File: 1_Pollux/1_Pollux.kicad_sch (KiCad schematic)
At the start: 0 parts

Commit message: feat: add schematic and pcb basis for right part
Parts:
- added J1: Conn_01x02, Connector_JST:JST_PH_S2B-PH-K_1x02_P2.00mm_Horizontal, symbol Connector_Generic:Conn_01x02
- added SW1: Battery Switch, davidphilipbarr:SPDT_C128955, symbol ScottoKeebs:Placeholder_Switch
- added SW2: LED Switch, davidphilipbarr:SPDT_C128955, symbol ScottoKeebs:Placeholder_Switch
- added SW3: Reset Switch, Button_Switch_SMD:Panasonic_EVQPUL_EVQPUC, symbol ScottoKeebs:Placeholder_Switch
- added U1: Nice_Nano_V2, ScottoKeebs_MCU:Nice_Nano_V2, symbol ScottoKeebs:MCU_Nice_Nano_V2
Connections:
- new net Column 0: U1.5 (2)
- new net Column 1: U1.6 (3)
- new net Column 2: U1.7 (4)
- new net Column 3: U1.8 (5)
- new net Column 4: U1.9 (6)
- new net Column 5: U1.10 (7)
- new net Column 6: U1.11 (8)
- new net Column 7: U1.12 (9)
- new net GND: J1.1 (Pin_1), SW3.1, U1.23 (GND), U1.3 (GND), U1.4 (GND)
- new net LED IN: U1.1
- new net POS: J1.2 (Pin_2), SW1.1
- new net RAW: SW1.2, SW2.1, U1.24 (B+)
- new net RST: SW3.2, U1.22 (RST)
- new net Row 0: U1.20 (21)
- new net Row 1: U1.19 (20)
- new net Row 2: U1.18 (19)
- new net Row 3: U1.17 (18)
- new net Row 4: U1.16 (15)
- new net Row 5: U1.15 (14)
- new net Row 6: U1.14 (16)
- new net Row 7: U1.13 (10)
- new net VDD: SW2.2
- no-connect marks 0 -> 5
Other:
- added sheet Keyswitches (_keyswitches.kicad_sch)
- added sheet LEDs (_leds.kicad_sch)

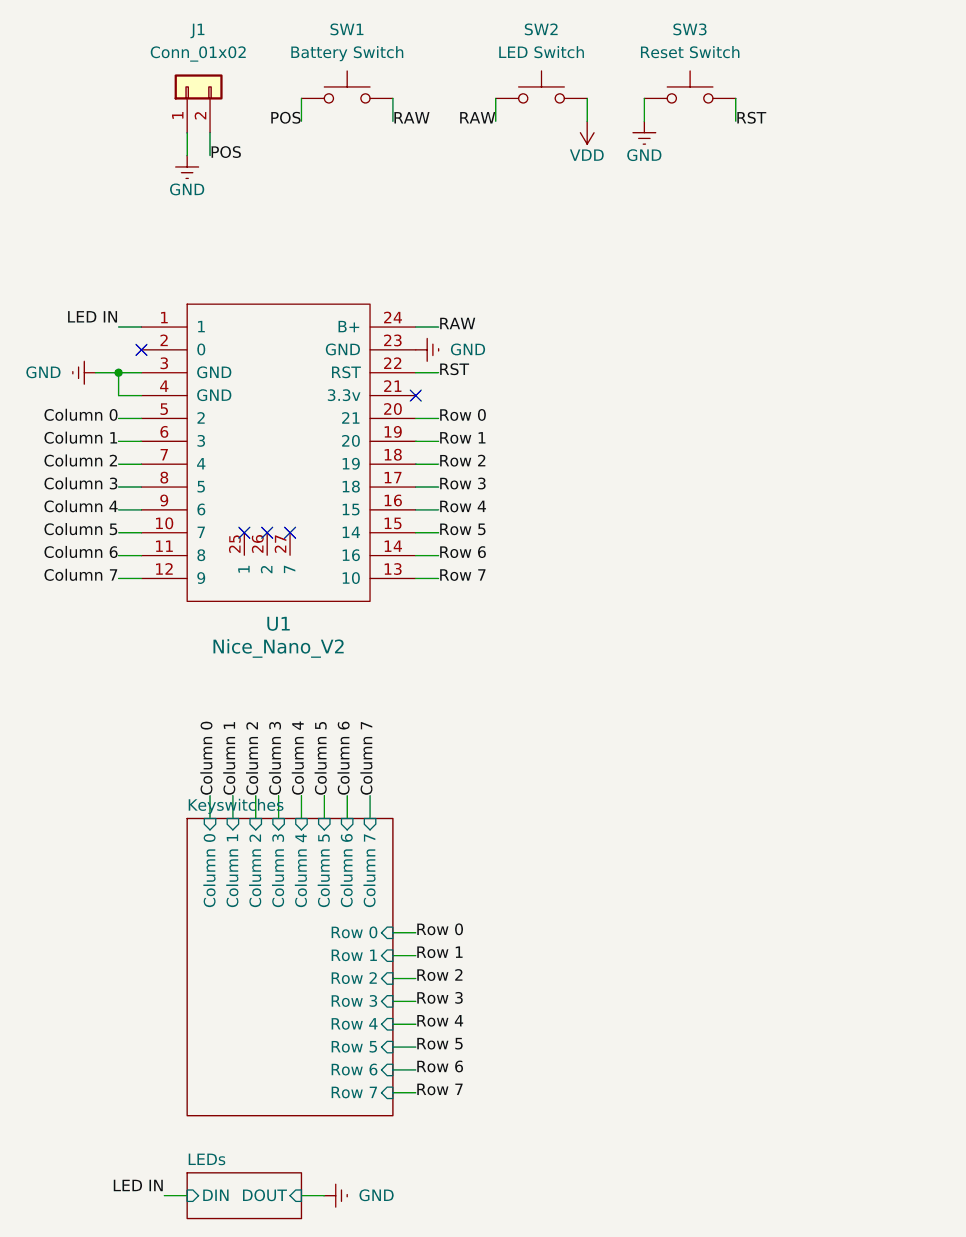
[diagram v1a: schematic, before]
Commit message: feat: finish Pollux PCB | chore: generate gerber files for both sides
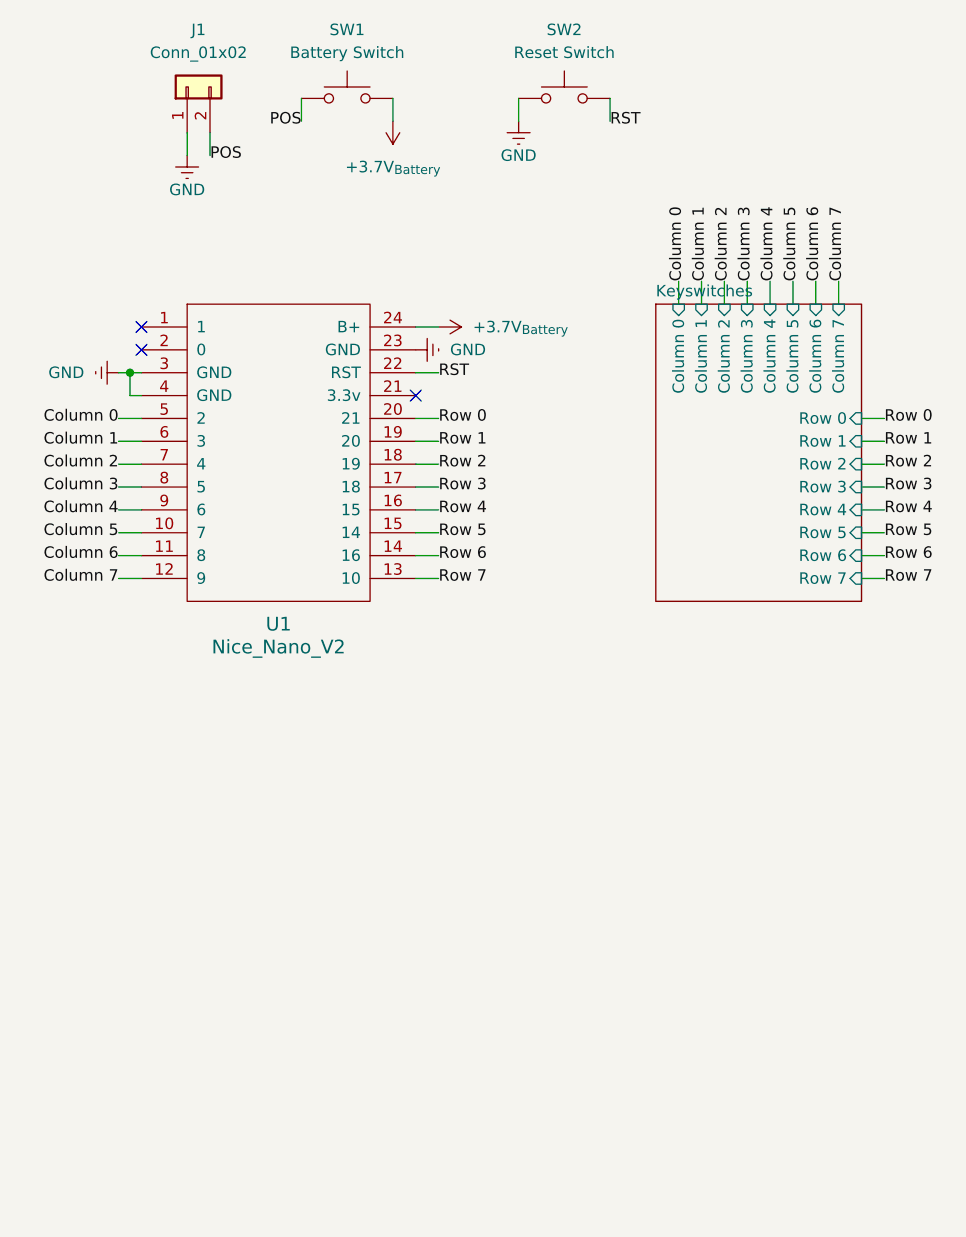
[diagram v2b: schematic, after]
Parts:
- removed SW2: LED Switch, davidphilipbarr:SPDT_C128955, symbol ScottoKeebs:Placeholder_Switch
- renumbered SW3 to SW2
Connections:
- net LED IN: no longer names the net of U1.1
- net RAW renamed +3.7V_{Battery}
- no-connect marks 5 -> 3
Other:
- removed sheet LEDs
- moved on the sheet: SW2
